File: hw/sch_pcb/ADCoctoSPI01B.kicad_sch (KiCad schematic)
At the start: 79 parts, among them J1 +5V, J10 HEADER_1x02, J11 HEADER_2x04, J2 SATA7-67491-1030, J3 SATA7-67491-1030, J4 SATA7-67491-1030, J5 SATA7-67491-1030, J7 SATA7-67491-1030, J8 HEADER_1x02, J9 HEADER_1x02, M1 HOLE, M2 HOLE, M3 HOLE, M4 HOLE, U1 AFE5801, U2 LM1117MP-1,8/NO, U3 LM1117MP-3,3/NO

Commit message: Edit PCB
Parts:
- C10, C11, C12, C13, C14, C15, C16, C17, C18, C19, C2, C20, C21, C22, C23, C24, C25, C26, C27, C28, C29, C3, C33, C34, C35, C36, C37, C38, C39, C4, C5, C6, C7, C8, C9: footprint Mlab_C:SMD-0603_narrow -> Capacitor_SMD:C_0603_1608Metric
- C30, C31: footprint Mlab_R:SMD-0805 -> Capacitor_SMD:C_0805_2012Metric
- J6: value (none) -> SAS_mini_1888174; footprint (none) -> Connector_SATA_SAS:SAS-mini_TEConnectivity_1888174_Vertical
- R1, R10, R11, R12, R13, R14, R15, R16, R17, R2, R20, R21, R3, R4, R5, R6, R7, R8, R9: footprint Mlab_R:SMD-0603 -> Resistor_SMD:R_0603_1608Metric
- U2, U3: footprint TO_SOT_Packages_SMD:SOT-223-3_TabPin2 -> Package_TO_SOT_SMD:SOT-223-3_TabPin2

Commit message: Edit footprints + 3d models
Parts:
- C1: footprint Capacitors_SMD:C_1210_HandSoldering -> Capacitor_SMD:C_1210_3225Metric_Pad1.33x2.70mm_HandSolder
- D1: footprint Diodes_SMD:D_SMA -> Diode_SMD:D_SMA
- L2, L3, L6: footprint Mlab_R:SMD-0805 -> Inductor_SMD:L_0805_2012Metric_Pad1.15x1.40mm_HandSolder
- M1, M2, M3, M4: footprint VIAS:MountingHole_3mm -> Mlab_Mechanical:MountingHole_3mm
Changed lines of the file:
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@@
       (effects (font (size 1.524 1.524)) hide)
     )
-    (property "Footprint" "VIAS:MountingHole_3mm" (id 2) (at 255.27 48.26 0)
+    (property "Footprint" "Mlab_Mechanical:MountingHole_3mm" (id 2) (at 255.27 48.26 0)
       (effects (font (size 1.524 1.524)) hide)
     )
@@
       (effects (font (size 1.524 1.524)) hide)
     )
-    (property "Footprint" "VIAS:MountingHole_3mm" (id 2) (at 260.35 48.26 0)
+    (property "Footprint" "Mlab_Mechanical:MountingHole_3mm" (id 2) (at 260.35 48.26 0)
       (effects (font (size 1.524 1.524)) hide)
     )
@@
       (effects (font (size 1.524 1.524)) hide)
     )
-    (property "Footprint" "VIAS:MountingHole_3mm" (id 2) (at 265.43 48.26 0)
+    (property "Footprint" "Mlab_Mechanical:MountingHole_3mm" (id 2) (at 265.43 48.26 0)
       (effects (font (size 1.524 1.524)) hide)
     )
@@
       (effects (font (size 1.524 1.524)) hide)
     )
-    (property "Footprint" "VIAS:MountingHole_3mm" (id 2) (at 270.51 48.26 0)
+    (property "Footprint" "Mlab_Mechanical:MountingHole_3mm" (id 2) (at 270.51 48.26 0)
       (effects (font (size 1.524 1.524)) hide)
     )
@@
       (effects (font (size 1.27 1.27)) (justify right))
     )
-    (property "Footprint" "Diodes_SMD:D_SMA" (id 2) (at 252.73 30.48 90)
+    (property "Footprint" "Diode_SMD:D_SMA" (id 2) (at 252.73 30.48 90)
       (effects (font (size 1.524 1.524)) hide)
     )
@@
       (effects (font (size 1.27 1.27)) (justify left))
     )
-    (property "Footprint" "Capacitors_SMD:C_1210_HandSoldering" (id 2) (at 237.49 30.48 0)
+    (property "Footprint" "Capacitor_SMD:C_1210_3225Metric_Pad1.33x2.70mm_HandSolder" (id 2) (at 237.49 30.48 0)
       (effects (font (size 1.524 1.524)) hide)
     )
@@
     (property "Reference" "L3" (id 0) (at 260.35 64.77 90))
     (property "Value" "BLM21PG300SN1D" (id 1) (at 256.54 67.31 90))
-    (property "Footprint" "Mlab_R:SMD-0805" (id 2) (at 260.985 69.85 0)
+    (property "Footprint" "Inductor_SMD:L_0805_2012Metric_Pad1.15x1.40mm_HandSolder" (id 2) (at 260.985 69.85 0)
       (effects (font (size 1.27 1.27)) hide)
     )
@@
     (property "Reference" "L2" (id 0) (at 260.985 92.075 90))
     (property "Value" "BLM21PG300SN1D" (id 1) (at 257.81 88.9 90))
-    (property "Footprint" "Mlab_R:SMD-0805" (id 2) (at 260.985 90.805 0)
+    (property "Footprint" "Inductor_SMD:L_0805_2012Metric_Pad1.15x1.40mm_HandSolder" (id 2) (at 260.985 90.805 0)
       (effects (font (size 1.27 1.27)) hide)
     )
@@
     (property "Reference" "L6" (id 0) (at 85.725 184.15 90))
     (property "Value" "BLM21PG300SN1D" (id 1) (at 82.55 180.975 90))
-    (property "Footprint" "Mlab_R:SMD-0805" (id 2) (at 85.725 182.88 0)
+    (property "Footprint" "Inductor_SMD:L_0805_2012Metric_Pad1.15x1.40mm_HandSolder" (id 2) (at 85.725 182.88 0)
       (effects (font (size 1.27 1.27)) hide)
     )
@@
     )
     (path "/00000000-0000-0000-0000-000055623093"
-      (reference "C1") (unit 1) (value "100uF/10V") (footprint "Capacitors_SMD:C_1210_HandSoldering")
+      (reference "C1") (unit 1) (value "100uF/10V") (footprint "Capacitor_SMD:C_1210_3225Metric_Pad1.33x2.70mm_HandSolder")
     )
     (path "/00000000-0000-0000-0000-000059daa64d"
@@
     )
     (path "/00000000-0000-0000-0000-000055622fb7"
-      (reference "D1") (unit 1) (value "M4") (footprint "Diodes_SMD:D_SMA")
+      (reference "D1") (unit 1) (value "M4") (footprint "Diode_SMD:D_SMA")
     )
     (path "/00000000-0000-0000-0000-0000549d65bc"
@@
     )
     (path "/00000000-0000-0000-0000-000059a25c29"
-      (reference "L2") (unit 1) (value "BLM21PG300SN1D") (footprint "Mlab_R:SMD-0805")
+      (reference "L2") (unit 1) (value "BLM21PG300SN1D") (footprint "Inductor_SMD:L_0805_2012Metric_Pad1.15x1.40mm_HandSolder")
     )
     (path "/00000000-0000-0000-0000-000059a254af"
-      (reference "L3") (unit 1) (value "BLM21PG300SN1D") (footprint "Mlab_R:SMD-0805")
+      (reference "L3") (unit 1) (value "BLM21PG300SN1D") (footprint "Inductor_SMD:L_0805_2012Metric_Pad1.15x1.40mm_HandSolder")
     )
     (path "/00000000-0000-0000-0000-00005a9b9cf9"
-      (reference "L6") (unit 1) (value "BLM21PG300SN1D") (footprint "Mlab_R:SMD-0805")
+      (reference "L6") (unit 1) (value "BLM21PG300SN1D") (footprint "Inductor_SMD:L_0805_2012Metric_Pad1.15x1.40mm_HandSolder")
     )
     (path "/00000000-0000-0000-0000-0000549d7549"
-      (reference "M1") (unit 1) (value "HOLE") (footprint "VIAS:MountingHole_3mm")
+      (reference "M1") (unit 1) (value "HOLE") (footprint "Mlab_Mechanical:MountingHole_3mm")
     )
     (path "/00000000-0000-0000-0000-0000549d7628"
-      (reference "M2") (unit 1) (value "HOLE") (footprint "VIAS:MountingHole_3mm")
+      (reference "M2") (unit 1) (value "HOLE") (footprint "Mlab_Mechanical:MountingHole_3mm")
     )
     (path "/00000000-0000-0000-0000-0000549d7646"
-      (reference "M3") (unit 1) (value "HOLE") (footprint "VIAS:MountingHole_3mm")
+      (reference "M3") (unit 1) (value "HOLE") (footprint "Mlab_Mechanical:MountingHole_3mm")
     )
     (path "/00000000-0000-0000-0000-0000549d7665"
-      (reference "M4") (unit 1) (value "HOLE") (footprint "VIAS:MountingHole_3mm")
+      (reference "M4") (unit 1) (value "HOLE") (footprint "Mlab_Mechanical:MountingHole_3mm")
     )
     (path "/00000000-0000-0000-0000-00005999d4eb"

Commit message: Edit footprint AFE5801
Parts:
- U1: footprint Mlab_IO:QFN-64-1EP_9x9mm_Pitch0.5mm -> Mlab_IO:VQFN-64_9.15x9.15mm_EP_7.5x7.5mm
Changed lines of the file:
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@@
       (effects (font (size 1.524 1.524)))
     )
-    (property "Footprint" "Mlab_IO:QFN-64-1EP_9x9mm_Pitch0.5mm" (id 2) (at 99.695 62.23 0)
+    (property "Footprint" "Mlab_IO:VQFN-64_9.15x9.15mm_EP_7.5x7.5mm" (id 2) (at 99.695 62.23 0)
       (effects (font (size 1.524 1.524)) hide)
     )
@@
     )
     (path "/00000000-0000-0000-0000-00005999bbf0"
-      (reference "U1") (unit 1) (value "AFE5801") (footprint "Mlab_IO:QFN-64-1EP_9x9mm_Pitch0.5mm")
+      (reference "U1") (unit 1) (value "AFE5801") (footprint "Mlab_IO:VQFN-64_9.15x9.15mm_EP_7.5x7.5mm")
     )
     (path "/00000000-0000-0000-0000-000059a1f3e1"

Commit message: Edit bom
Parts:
- C1: value 100uF/10V -> 100uF/6V3; UST_ID (none) -> 5c70984812875079b91f8bbb
- C10, C11, C12, C13, C14, C15, C16, C17, C18, C3, C4, C5, C6, C7, C8, C9: UST_ID (none) -> 5c70984812875079b91f8bef
- C19, C2, C20, C21, C22, C23, C24, C26, C27, C28, C29, C33, C34, C35, C36, C37, C38, C39: UST_ID (none) -> 5c70984812875079b91f8bf2
- C25: value 100n -> 100nF; UST_ID (none) -> 5c70984812875079b91f8bf2
- C30, C31: UST_ID (none) -> 5c70984812875079b91f8bbd
- D1: UST_ID (none) -> 5c70984512875079b91f88ac
- J2, J3, J4, J5, J7: UST_ID (none) -> 5c70984712875079b91f8a7b
- J6: UST_ID (none) -> 624ede60592c2d62176d5a96
- L2, L3, L6: UST_ID (none) -> 5c70984412875079b91f87fd
- R1, R2, R3, R4, R5, R6, R7, R8, R9: UST_ID (none) -> 5c70984512875079b91f8956
- R10, R20: value 127 -> 130; UST_ID (none) -> 5cd08b17128750448e4542b1
- R11, R21: value 83 -> 82; UST_ID (none) -> 5c70984512875079b91f8955
- R12, R13, R14, R15, R16, R17: UST_ID (none) -> 5c70984512875079b91f8962
- U1: UST_ID (none) -> 624edf21592c2d62176d5abc
- U2: UST_ID (none) -> 5c70984712875079b91f8af6
- U3: UST_ID (none) -> 5c70984712875079b91f8af9

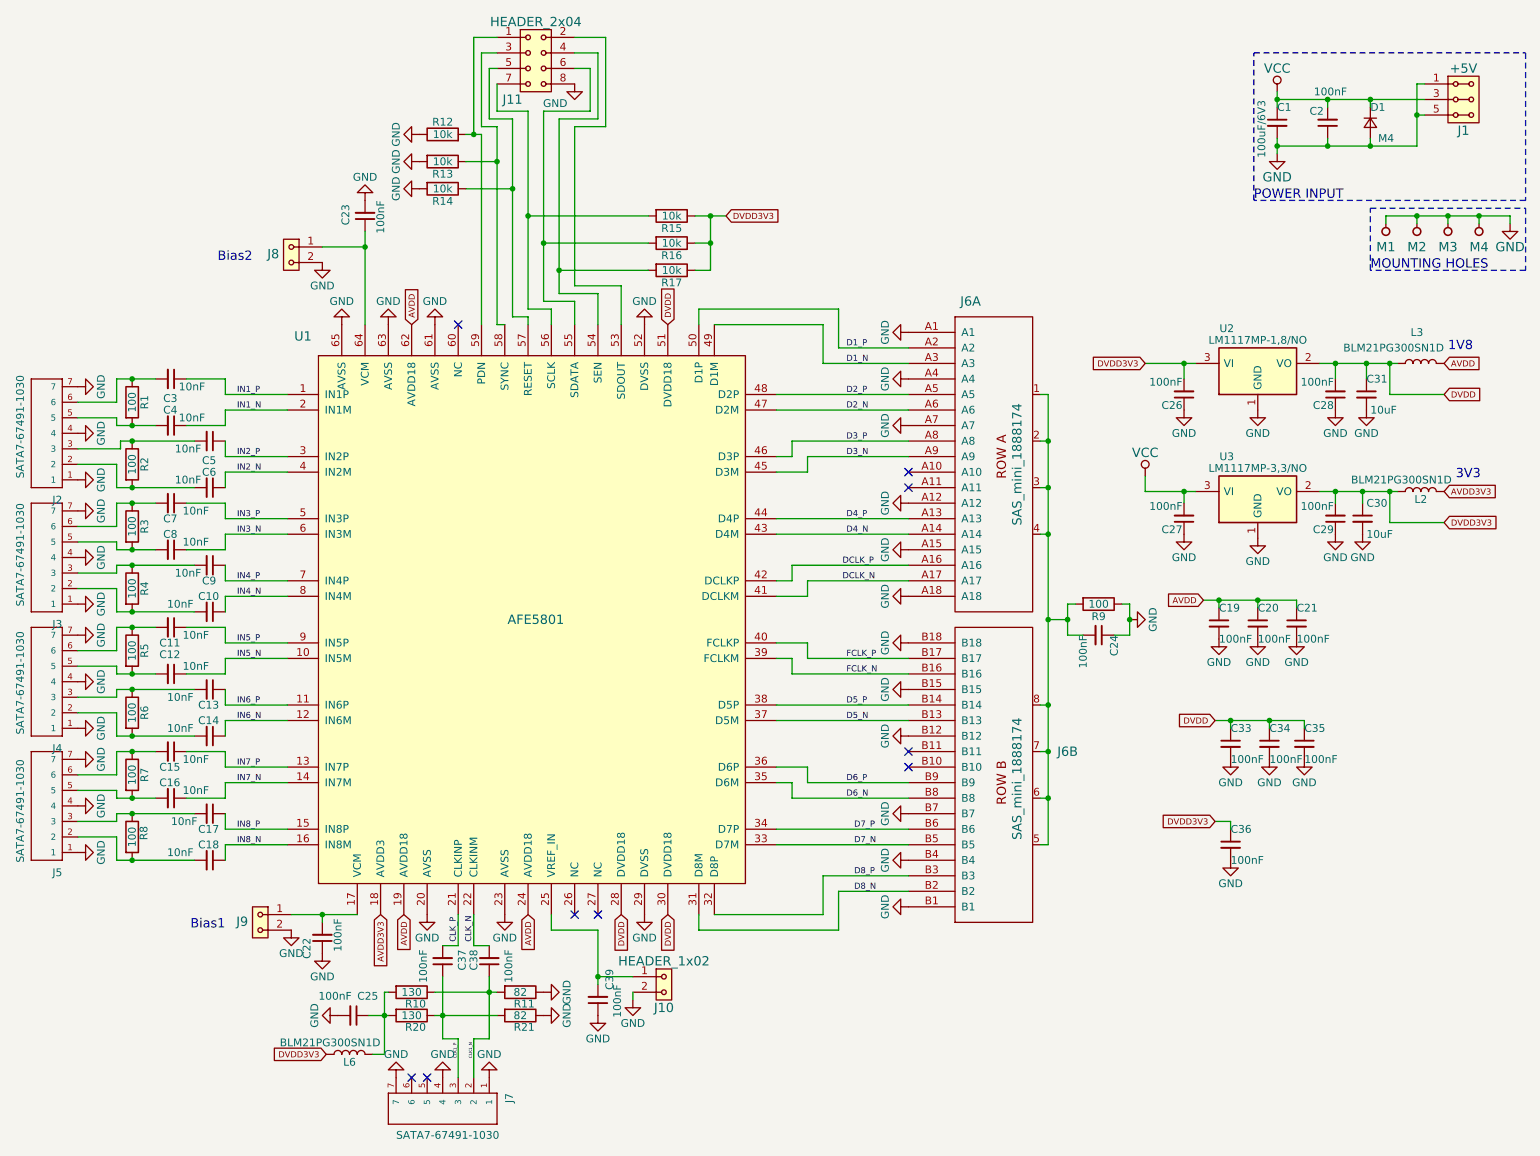
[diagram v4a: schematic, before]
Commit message: rozdeleni VSSA a VSSD
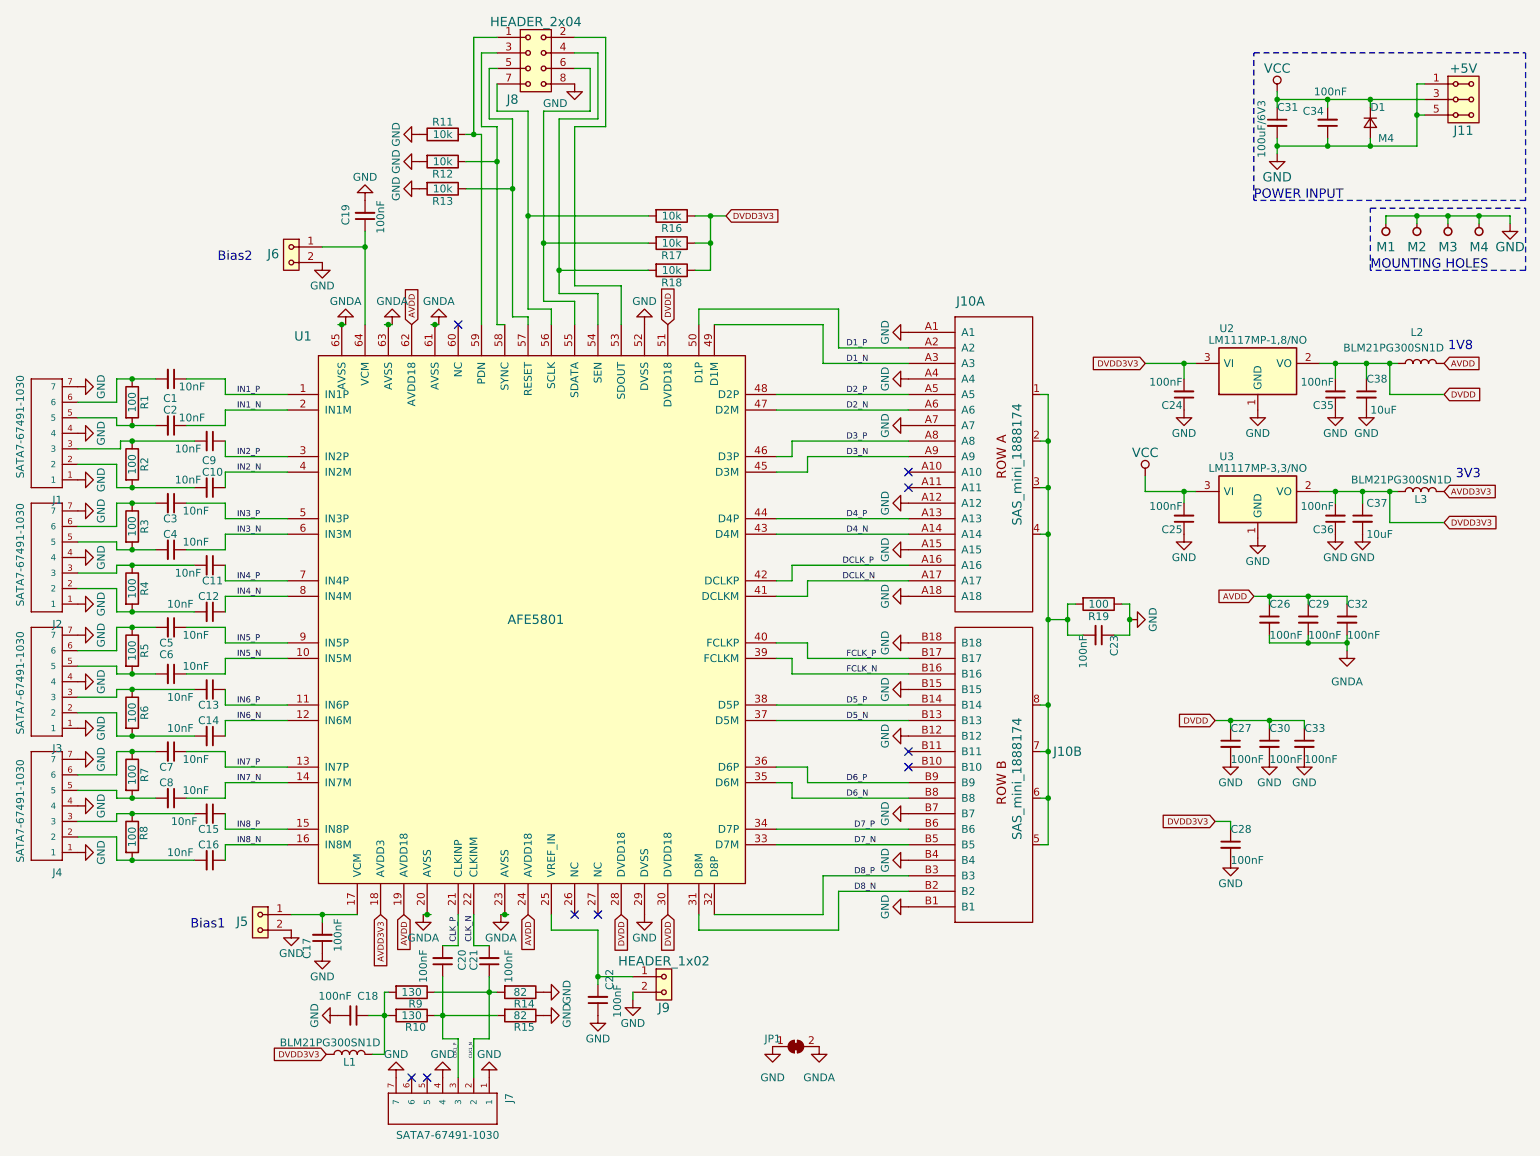
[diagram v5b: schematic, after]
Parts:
- added JP1: SolderJumper_2_Bridged, NetTie:NetTie-2_SMD_Pad0.5mm, symbol Jumper:SolderJumper_2_Bridged
- renumbered C3 to C1, C6 to C10, C9 to C11, C10 to C12, C17 to C15, C18 to C16, C22 to C17, C25 to C18, C23 to C19, C4 to C2, C37 to C20, C38 to C21, C39 to C22, C24 to C23, C26 to C24, C27 to C25, C19 to C26, C33 to C27, C36 to C28, C20 to C29, C7 to C3, C34 to C30, C1 to C31, C21 to C32, C35 to C33, C2 to C34, C28 to C35, C29 to C36, C30 to C37, C31 to C38, C8 to C4, C11 to C5, C12 to C6, C15 to C7, C16 to C8, C5 to C9, J2 to J1, J6 to J10, J1 to J11, J3 to J2, J4 to J3, J5 to J4, J9 to J5, J8 to J6, J11 to J8, J10 to J9, L6 to L1, L3 to L2, L2 to L3, R20 to R10, R12 to R11, R13 to R12, R14 to R13, R11 to R14, R21 to R15, R15 to R16, R16 to R17, R17 to R18, R9 to R19, R10 to R9
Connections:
- net GND: now also JP1.1 (A); no longer C26.2, C29.2, C32.2, U1.20 (AVSS), U1.23 (AVSS), U1.61 (AVSS), U1.63 (AVSS), U1.65 (AVSS)
- new net GNDA: C26.2, C29.2, C32.2, JP1.2 (B), U1.20 (AVSS), U1.23 (AVSS), U1.61 (AVSS), U1.63 (AVSS), U1.65 (AVSS)
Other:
- moved on the sheet: C26, C29, C32

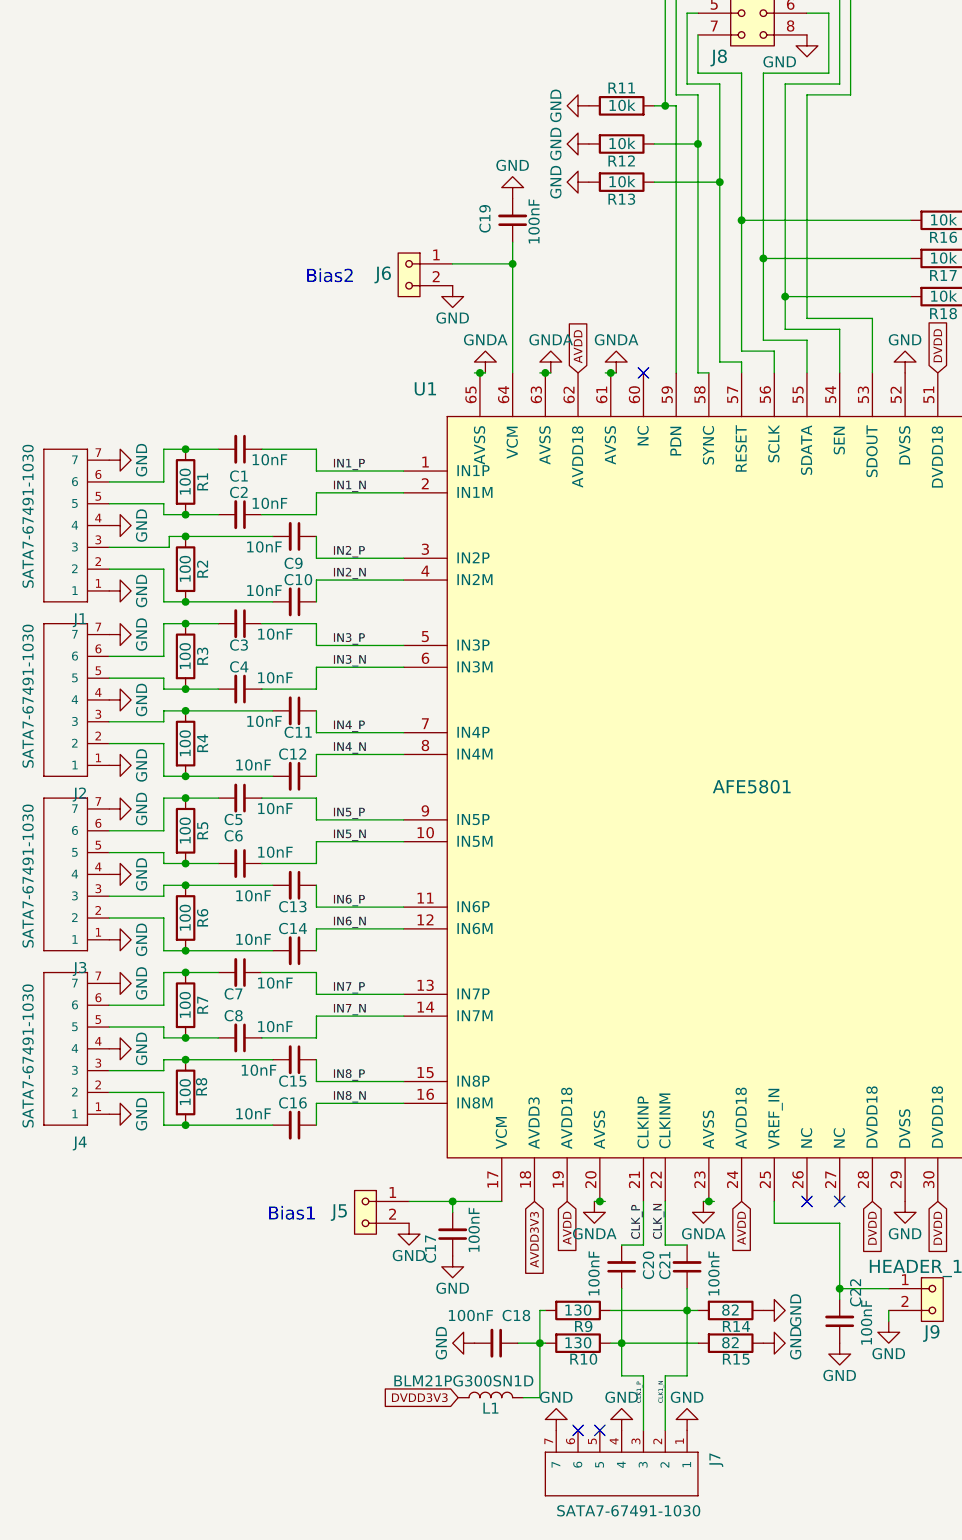
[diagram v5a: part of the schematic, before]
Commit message: uprava AGND
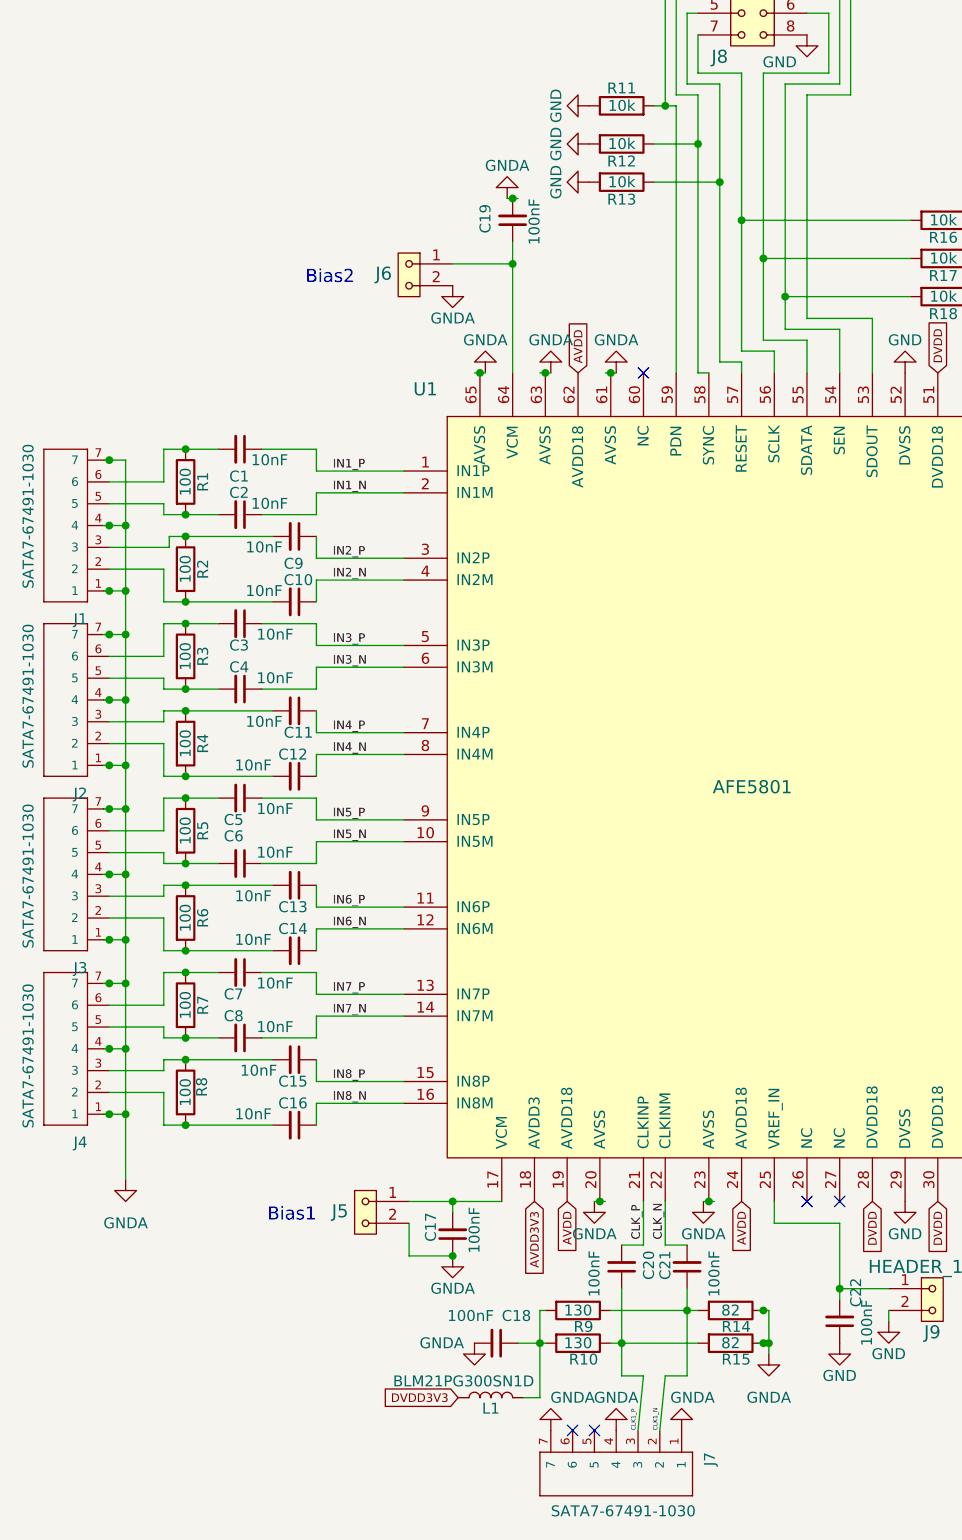
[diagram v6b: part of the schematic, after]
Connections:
- net GND: no longer C17.1, C18.2, C19.2, J1.1, J1.4, J1.7, J2.1, J2.4, J2.7, J3.1, J3.4, J3.7, J4.1, J4.4, J4.7, J5.2, J6.2, J7.1, J7.4, J7.7, R14.1, R15.1
- net GNDA: now also C17.1, C18.2, C19.2, J1.1, J1.4, J1.7, J2.1, J2.4, J2.7, J3.1, J3.4, J3.7, J4.1, J4.4, J4.7, J5.2, J6.2, J7.1, J7.4, J7.7, R14.1, R15.1
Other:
- moved on the sheet: J7
